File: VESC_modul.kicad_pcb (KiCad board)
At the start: 4 copper layers, 30 x 18 mm, 53 parts, among them U1 PINx6, U10 STM32F405RGTx, U2 PINx4, U3 PINx2, U4 PINx6, U5 PINx6, U6 PINx4, U7 PINx9, U8 DRV8320RS, U9 MCP1700-3.3V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

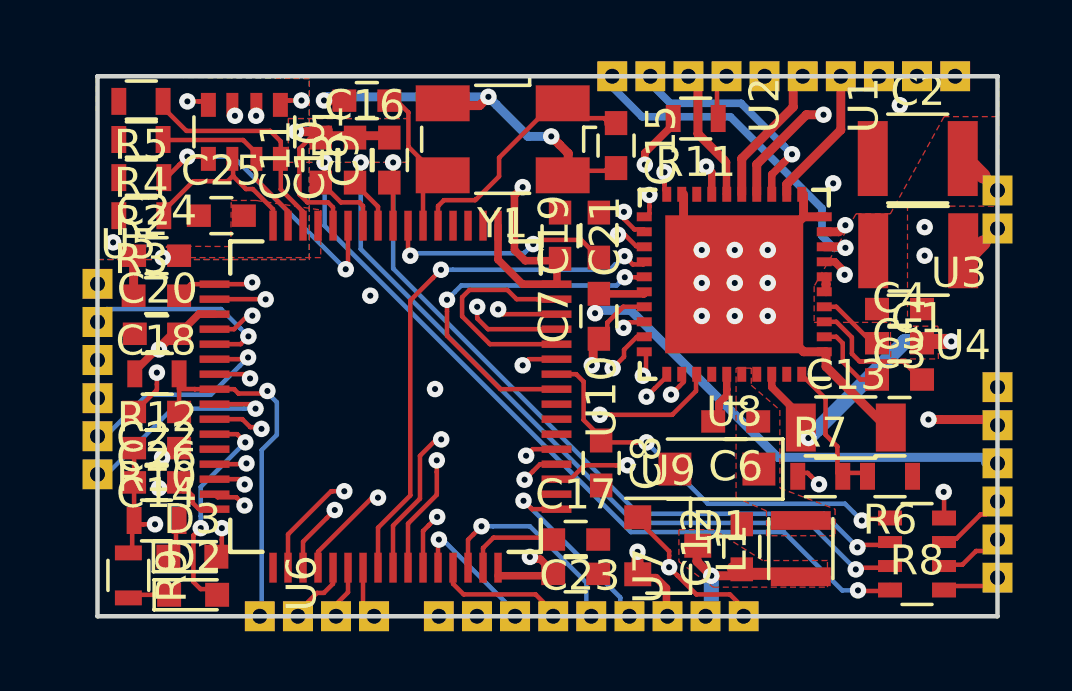
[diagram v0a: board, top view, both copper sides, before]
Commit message: improved GND
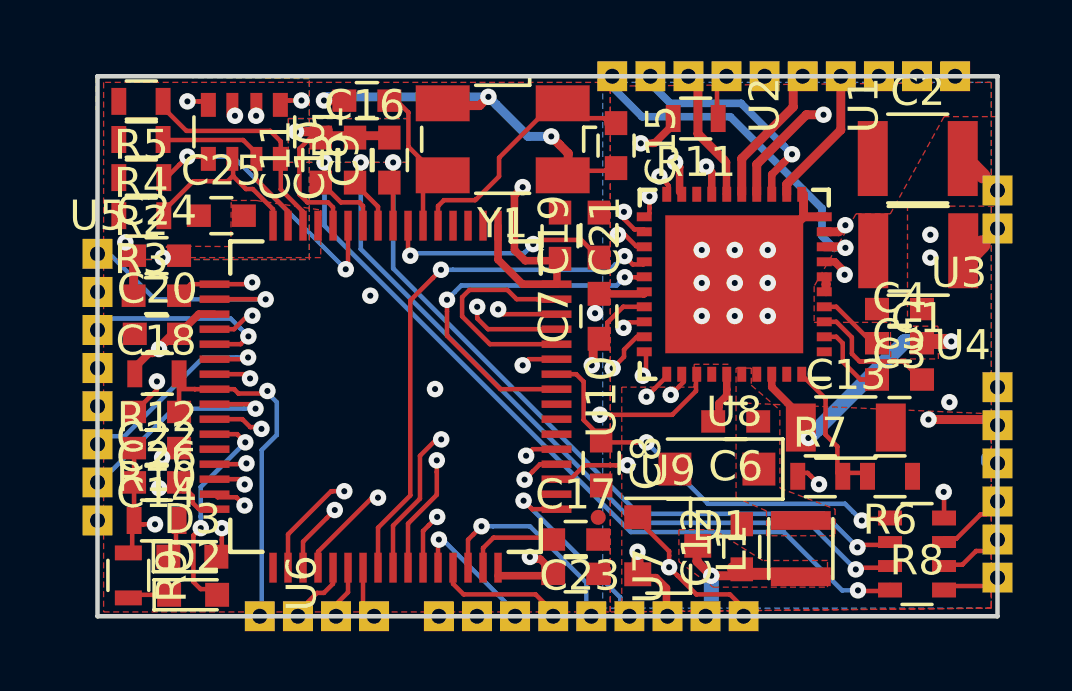
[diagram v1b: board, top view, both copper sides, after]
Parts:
- U5: value PINx6 -> PINx8; footprint user_defined:PINx6-1.27mm -> user_defined:PINx8-1.27mm
- moved U5 1.54 mm to (100.0, 113.5)
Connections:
- C1 pad 1: GND_EXT -> GNDD
- C2 pad 1: GND_EXT -> GNDD
- C3 pad 1: GND_EXT -> GNDD
- U3 pad 2: GND_EXT -> GNDD
- U5 pad 1: ADC_15_EXT -> AGND_EXT
- U5 pad 2: MISO_ADC2_EXT -> ADC_15_EXT
- U5 pad 3: TX_SCL_MOSI_EXT -> MISO_ADC2_EXT
- U5 pad 4: RX_SDA_NSS_EXT -> TX_SCL_MOSI_EXT
- U5 pad 5: SCK_ADC_EXT -> RX_SDA_NSS_EXT
- U5 pad 6: PWM_EXT -> SCK_ADC_EXT
- U8 pad 1: GND_EXT -> GNDD
- U8 pad 10: GND_EXT -> GNDD
- U8 pad 11: GND_EXT -> GNDD
- U8 pad 18: GND_EXT -> GNDD
- U8 pad 41: GND_EXT -> GNDD
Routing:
- net AGND_EXT: track 55.2 -> 60.3 mm, vias 4 -> 5
- net GNDD: track 0.00 -> 4.27 mm, vias 0 -> 11
- net GND_EXT: track 54.0 -> 51.0 mm, vias 21 -> 9
- added copper zone on B.Cu, net GNDD
- added copper zone on F.Cu, net GNDD
- added copper zone on In1.Cu, net GNDD
- added copper zone on In2.Cu, net GNDD
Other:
- board text added: "GND SERVO ADC1 RX TX ADC2 ADC3 AGND"
- board text removed: "SERVO ADC1 RX TX ADC2 ADC3"
